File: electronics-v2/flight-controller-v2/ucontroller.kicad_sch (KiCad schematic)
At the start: 46 parts, among them J10 Conn_01x05, J11 Conn_01x06, J8 USB_B_Micro, J9 Conn_01x05, SW2 SW_Push, SW3 SW_Push, U4 STM32F411RETx, U5 ESP-12E, Y1 8MHz

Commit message: fixes in routing
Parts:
- removed J9: Conn_01x05, goose:tht_pin_01x05, symbol Connector_Generic:Conn_01x05
- added J11: Conn_02x03_Odd_Even, Connector_IDC:IDC-Header_2x03_P2.54mm_Vertical, symbol Connector_Generic:Conn_02x03_Odd_Even
- added J9: Conn_02x04_Odd_Even, goose:tht_pin_02x04, symbol Connector_Generic:Conn_02x04_Odd_Even
- renumbered J11 to J10, J10 to J12
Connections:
- net +3.3V: now also J11.6 (Pin_6), J9.2 (Pin_2)
- net ESC_TIM1_CH2: now also U4.43 (PA10); no longer U4.42 (PA9)
- net ESP_UART1_RX: now also U4.55 (PB3); no longer U4.59 (PB7)
- net GND: now also J11.5 (Pin_5), J9.1 (Pin_1)
- net IMU_INT: now also U4.50 (PA15); no longer U4.56 (PB4)
- net LED_B: now also U4.33 (PB12); no longer U4.29 (PB10)
- net LED_G: now also U4.34 (PB13); no longer U4.33 (PB12)
- net LED_R: now also U4.35 (PB14); no longer U4.34 (PB13)
- net MAG_INT: now also U4.59 (PB7); no longer U4.57 (PB5)
- net VLX_INT: now also U4.42 (PA9), J11.2 (Pin_2); no longer U4.43 (PA10)
- net VLX_XSHUT: now also J11.1 (Pin_1)
- net NRF_IRQ: now reaches U4.54 (PD2)
- net NRF_IRQ: now also J9.8 (Pin_8)
- net EXT_I2C3_SCL renamed VLX_SCL
- net VLX_SCL: now also J11.4 (Pin_4)
- net EXT_I2C3_SDA renamed VLX_SDA
- net VLX_SDA: now also J11.3 (Pin_3)
- net PA0 renamed GPS_PPS
- net PA1 renamed GPS_EN
- net SPI3_MISO renamed NRF_MISO
- net NRF_MISO: now also J9.7 (Pin_7)
- net SPI3_MOSI renamed NRF_MOSI
- net NRF_MOSI: now also J9.6 (Pin_6)
- net SPI3_SCK renamed NRF_SCK
- net NRF_SCK: now also J9.5 (Pin_5)
- net UART2_RX renamed GPS_RX
- net UART2_TX renamed GPS_TX
- new net NRF_CE: J9.3 (Pin_3), U4.57 (PB5)
- new net NRF_CSN: J9.4 (Pin_4), U4.56 (PB4)
- no-connect marks 31 -> 28
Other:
- note added: "I2C address: 0x52"
- note added: "external sensors"
- note removed: "reserve"
- moved on the sheet: C23, J10, J12, J8

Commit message: generate schematic
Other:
- title: (none) -> UAV TVC Goose Flight Controller
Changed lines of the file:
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@@
 (kicad_sch (version 20211123) (generator eeschema)
   (paper "A4")
+  (title_block
+    (title "UAV TVC Goose Flight Controller")
+    (date "2023-07-31")
+    (rev "V2.0")
+  )
   (junction (at 250.19 120.65) (diameter 0) (color 0 0 0 0)
   )

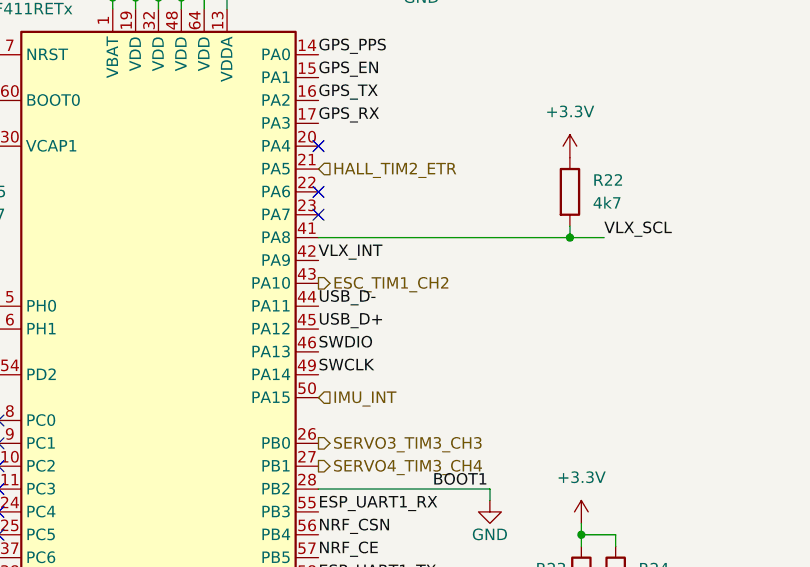
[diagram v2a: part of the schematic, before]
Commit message: fix route name, remove ADC code
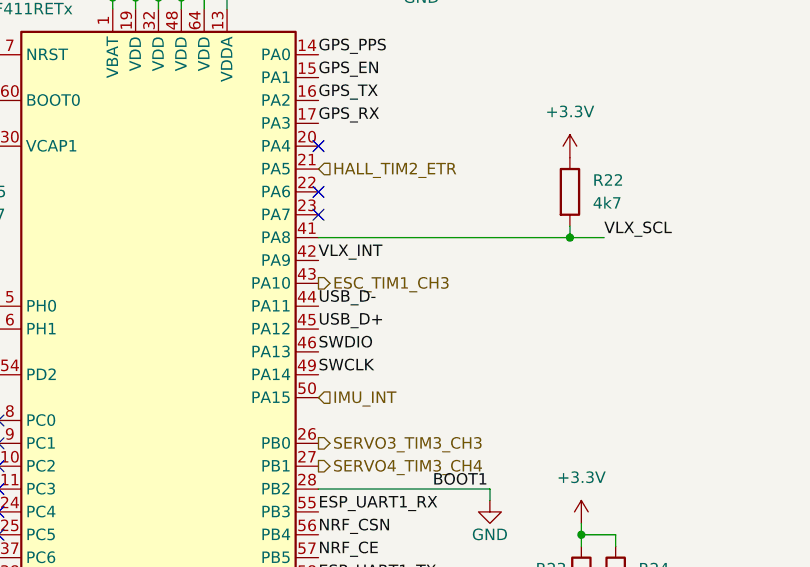
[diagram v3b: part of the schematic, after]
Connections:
- net ESC_TIM1_CH2 renamed ESC_TIM1_CH3
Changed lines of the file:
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@@
     (effects (font (size 1.27 1.27)) (justify right))
   )
-  (hierarchical_label "ESC_TIM1_CH2" (shape output) (at 113.03 106.68 0)
+  (hierarchical_label "ESC_TIM1_CH3" (shape output) (at 113.03 106.68 0)
     (effects (font (size 1.27 1.27)) (justify left))
   )
